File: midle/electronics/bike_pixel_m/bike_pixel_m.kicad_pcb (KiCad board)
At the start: 2 copper layers, 39 x 39 mm, 24 parts, among them J1 Battery, J2 Arduino, J3 Matrix, SW1 on/off, SW2 mode, SW3 color, SW4 effect, U1 MT3608

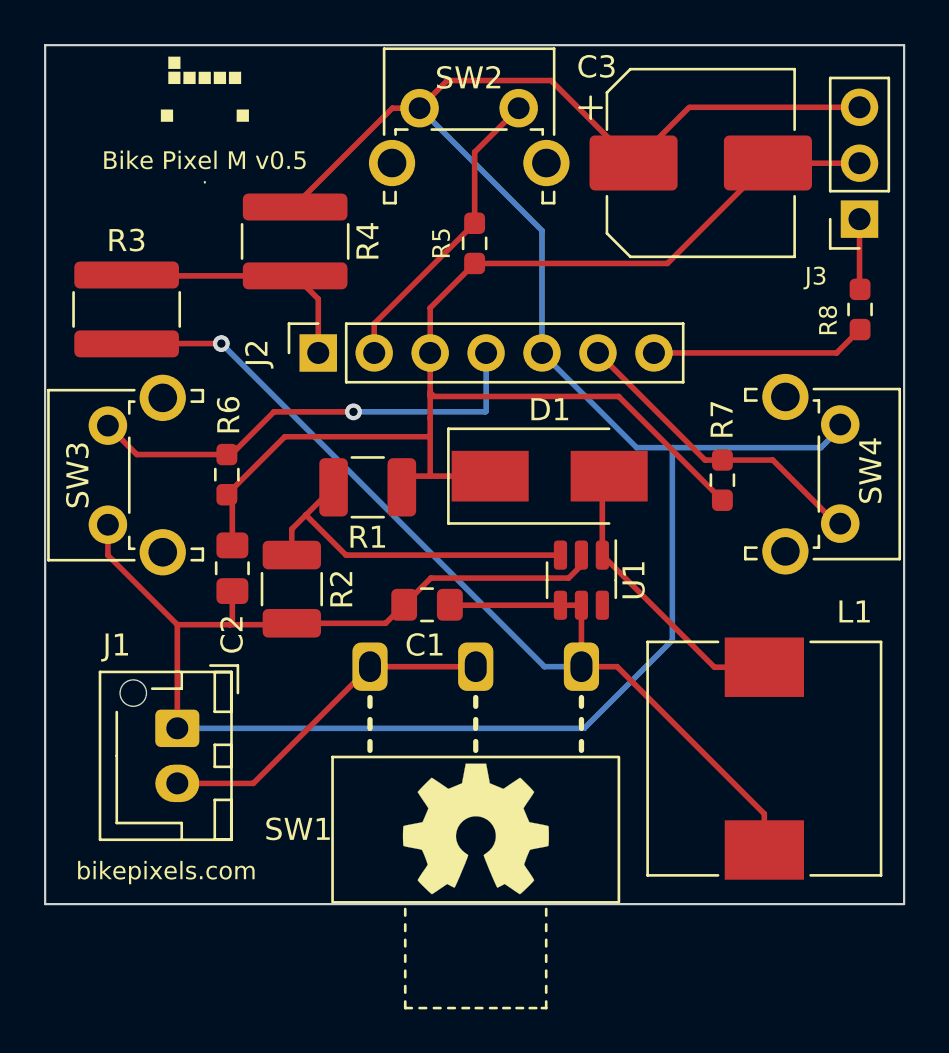
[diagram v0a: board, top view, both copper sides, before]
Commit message: Added Bike Pixel M PCB KiCad and production gerber files
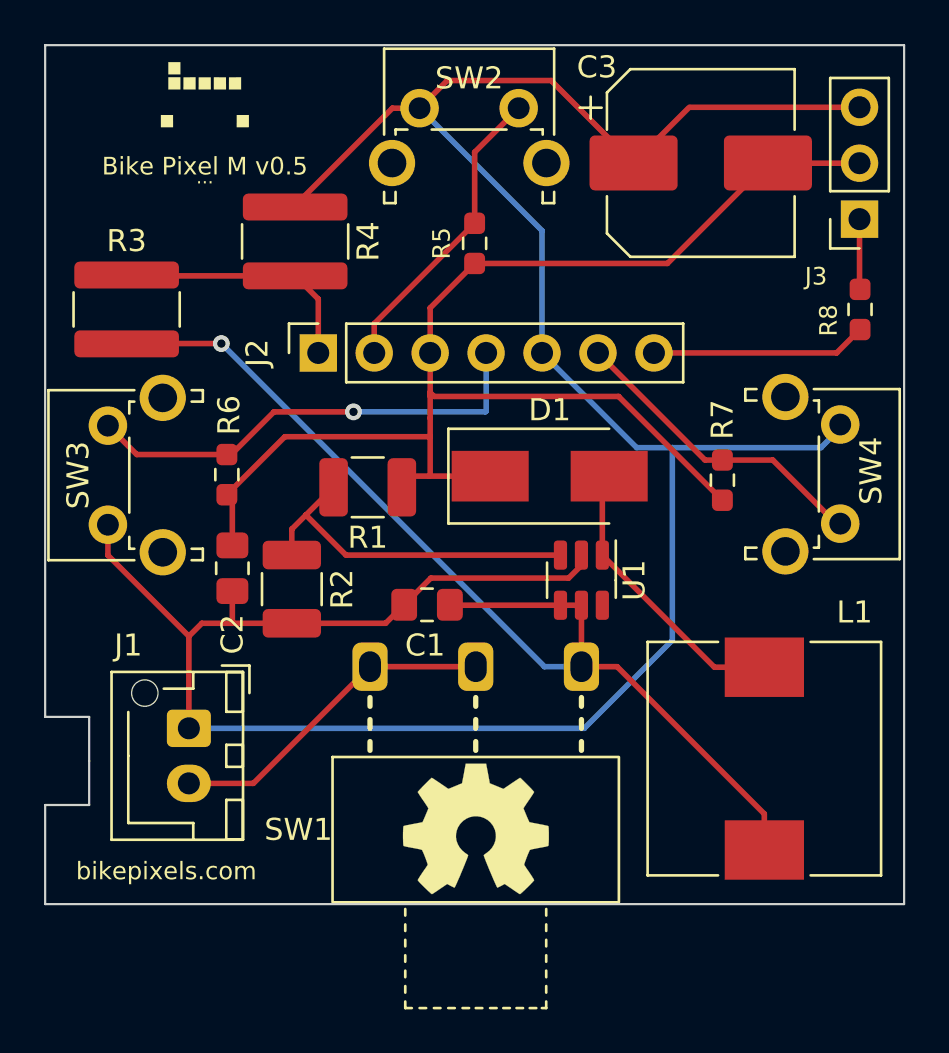
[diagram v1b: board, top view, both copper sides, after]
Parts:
- moved J1 0.52 mm to (126.5, 111.0)
- moved ... 0.25 mm to (127.2, 82.8)
- moved Bike Pixel M v0.5 0.25 mm to (127.2, 82.2)
- renumbered . to ...
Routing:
- net GND: track 124.8 -> 124.1 mm
- net Net-(J1-Pad2): track 15.7 -> 15.2 mm
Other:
- outline, holes or cut-outs redrawn
